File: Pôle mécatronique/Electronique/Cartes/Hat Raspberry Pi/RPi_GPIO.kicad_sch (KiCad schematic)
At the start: 1 part, among them J2 RPi_GPIO

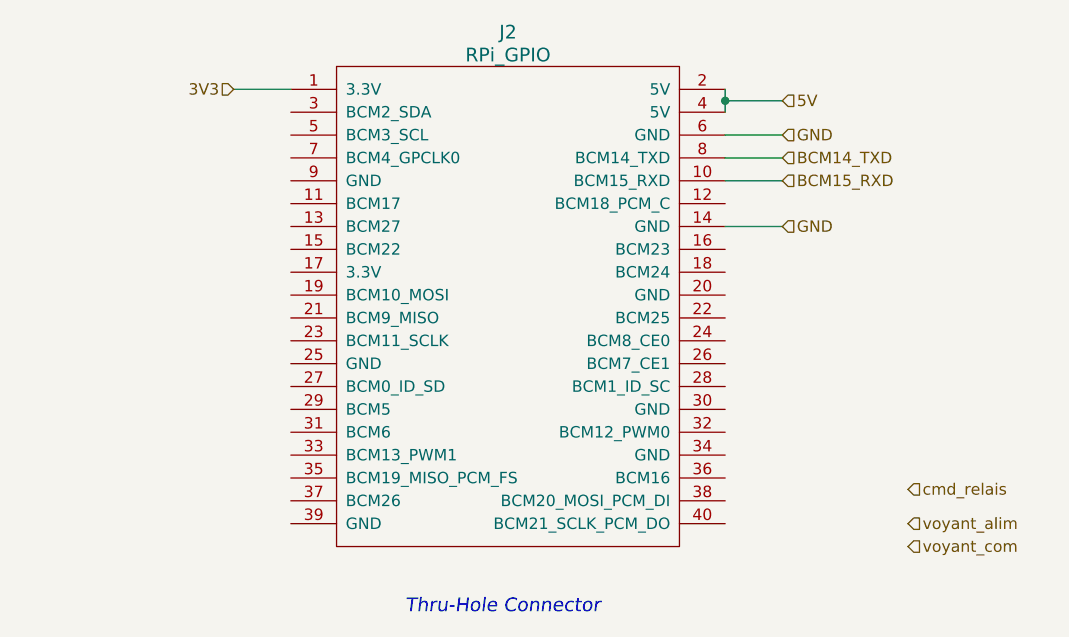
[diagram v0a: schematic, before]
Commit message: Update HAT RPI
- Ajout MCP25625
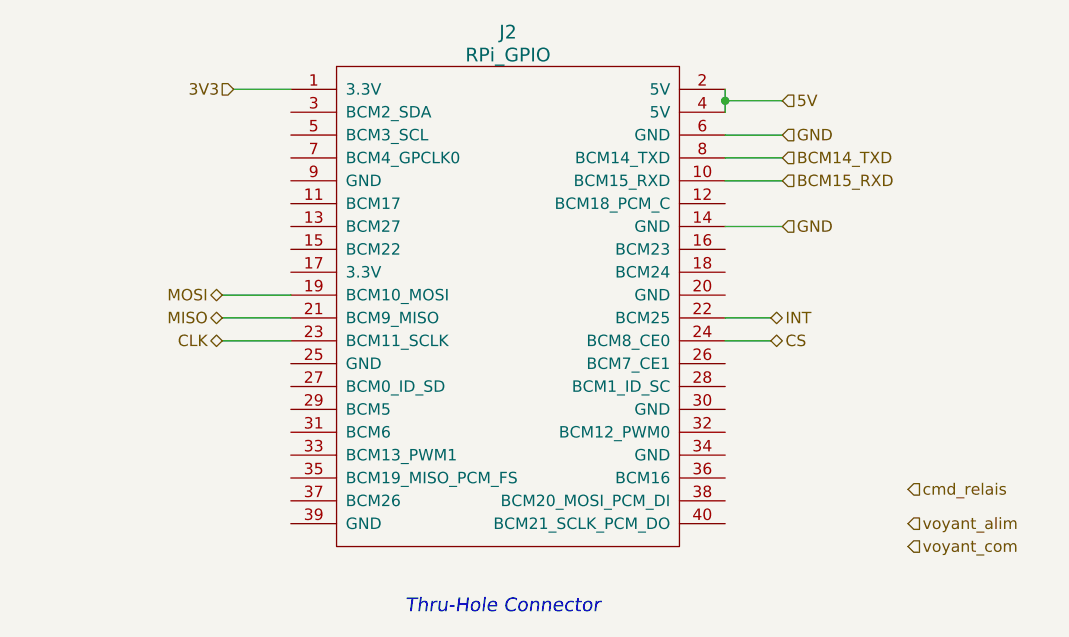
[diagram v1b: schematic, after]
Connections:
- net MOSI: now reaches J2.19 (BCM10_MOSI)
- net MISO: now reaches J2.21 (BCM9_MISO)
- net INT: now reaches J2.22 (BCM25)
- net CLK: now reaches J2.23 (BCM11_SCLK)
- net CS: now reaches J2.24 (BCM8_CE0)
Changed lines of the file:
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@@
+    (stroke (width 0) (type default) (color 0 0 0 0))
+  )
+  (wire (pts (xy 233.68 93.98) (xy 238.76 93.98))
     (stroke (width 0) (type default) (color 0 0 0 0))
   )
@@
     (stroke (width 0) (type default) (color 0 0 0 0))
   )
+  (wire (pts (xy 177.8 91.44) (xy 185.42 91.44))
+    (stroke (width 0) (type default) (color 0 0 0 0))
+  )
   (wire (pts (xy 233.68 68.58) (xy 233.68 69.85))
     (stroke (width 0) (type default) (color 0 0 0 0))
   )
+  (wire (pts (xy 177.8 96.52) (xy 185.42 96.52))
+    (stroke (width 0) (type default) (color 0 0 0 0))
+  )
   (wire (pts (xy 233.68 73.66) (xy 240.03 73.66))
+    (stroke (width 0) (type default) (color 0 0 0 0))
+  )
+  (wire (pts (xy 177.8 93.98) (xy 185.42 93.98))
     (stroke (width 0) (type default) (color 0 0 0 0))
   )
@@
   )
   (wire (pts (xy 233.68 69.85) (xy 233.68 71.12))
+    (stroke (width 0) (type default) (color 0 0 0 0))
+  )
+  (wire (pts (xy 233.68 96.52) (xy 238.76 96.52))
     (stroke (width 0) (type default) (color 0 0 0 0))
   )
@@
     (effects (font (size 1.27 1.27)) (justify left))
   )
+  (hierarchical_label "INT" (shape bidirectional) (at 238.76 93.98 0)
+    (effects (font (size 1.27 1.27)) (justify left))
+  )
   (hierarchical_label "BCM14_TXD" (shape input) (at 240.03 76.2 0)
     (effects (font (size 1.27 1.27)) (justify left))
+  )
+  (hierarchical_label "CS" (shape bidirectional) (at 238.76 96.52 0)
+    (effects (font (size 1.27 1.27)) (justify left))
+  )
+  (hierarchical_label "MOSI" (shape bidirectional) (at 177.8 91.44 180)
+    (effects (font (size 1.27 1.27)) (justify right))
   )
   (hierarchical_label "GND" (shape input) (at 240.03 73.66 0)
@@
   (hierarchical_label "cmd_relais" (shape input) (at 254 113.03 0)
     (effects (font (size 1.27 1.27)) (justify left))
+  )
+  (hierarchical_label "CLK" (shape bidirectional) (at 177.8 96.52 180)
+    (effects (font (size 1.27 1.27)) (justify right))
   )
   (hierarchical_label "voyant_alim" (shape input) (at 254 116.84 0)
@@
     (effects (font (size 1.27 1.27)) (justify left))
   )
+  (hierarchical_label "MISO" (shape bidirectional) (at 177.8 93.98 180)
+    (effects (font (size 1.27 1.27)) (justify right))
+  )
   (hierarchical_label "5V" (shape input) (at 240.03 69.85 0)

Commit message: Update HAT
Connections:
- net GND: now also J2.25 (GND), J2.39 (GND), J2.9 (GND); no longer J2.14 (GND)
- net cmd_relais: now also J2.7 (BCM4_GPCLK0)
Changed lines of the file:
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@@
     (stroke (width 0) (type default) (color 0 0 0 0))
   )
-  (wire (pts (xy 233.68 83.82) (xy 240.03 83.82))
+  (wire (pts (xy 180.34 78.74) (xy 185.42 78.74))
     (stroke (width 0) (type default) (color 0 0 0 0))
   )
@@
     (stroke (width 0) (type default) (color 0 0 0 0))
   )
+  (wire (pts (xy 180.34 76.2) (xy 185.42 76.2))
+    (stroke (width 0) (type default) (color 0 0 0 0))
+  )
+  (wire (pts (xy 180.34 99.06) (xy 185.42 99.06))
+    (stroke (width 0) (type default) (color 0 0 0 0))
+  )
   (wire (pts (xy 177.8 93.98) (xy 185.42 93.98))
+    (stroke (width 0) (type default) (color 0 0 0 0))
+  )
+  (wire (pts (xy 181.61 116.84) (xy 185.42 116.84))
     (stroke (width 0) (type default) (color 0 0 0 0))
   )
@@
     (effects (font (size 1.27 1.27)) (justify left))
   )
-  (hierarchical_label "GND" (shape input) (at 240.03 83.82 0)
+  (hierarchical_label "INT" (shape bidirectional) (at 238.76 93.98 0)
     (effects (font (size 1.27 1.27)) (justify left))
   )
-  (hierarchical_label "INT" (shape bidirectional) (at 238.76 93.98 0)
-    (effects (font (size 1.27 1.27)) (justify left))
+  (hierarchical_label "GND" (shape input) (at 180.34 78.74 180)
+    (effects (font (size 1.27 1.27)) (justify right))
   )
   (hierarchical_label "BCM14_TXD" (shape input) (at 240.03 76.2 0)
@@
     (effects (font (size 1.27 1.27)) (justify left))
   )
-  (hierarchical_label "cmd_relais" (shape input) (at 254 113.03 0)
-    (effects (font (size 1.27 1.27)) (justify left))
+  (hierarchical_label "cmd_relais" (shape input) (at 180.34 76.2 180)
+    (effects (font (size 1.27 1.27)) (justify right))
+  )
+  (hierarchical_label "GND" (shape input) (at 180.34 99.06 180)
+    (effects (font (size 1.27 1.27)) (justify right))
   )
   (hierarchical_label "CLK" (shape bidirectional) (at 177.8 96.52 180)
     (effects (font (size 1.27 1.27)) (justify right))
   )
-  (hierarchical_label "voyant_alim" (shape input) (at 254 116.84 0)
-    (effects (font (size 1.27 1.27)) (justify left))
-  )
   (hierarchical_label "3V3" (shape input) (at 179.07 68.58 180)
     (effects (font (size 1.27 1.27)) (justify right))
   )
-  (hierarchical_label "voyant_com" (shape input) (at 254 119.38 0)
-    (effects (font (size 1.27 1.27)) (justify left))
+  (hierarchical_label "GND" (shape input) (at 181.61 116.84 180)
+    (effects (font (size 1.27 1.27)) (justify right))
   )
   (hierarchical_label "MISO" (shape bidirectional) (at 177.8 93.98 180)

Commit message: Update alim correction
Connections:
- net GND: no longer J2.39 (GND)
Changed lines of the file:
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@@
-    (stroke (width 0) (type default) (color 0 0 0 0))
-  )
-  (wire (pts (xy 181.61 116.84) (xy 185.42 116.84))
     (stroke (width 0) (type default) (color 0 0 0 0))
   )
@@
     (effects (font (size 1.27 1.27)) (justify right))
   )
-  (hierarchical_label "GND" (shape input) (at 181.61 116.84 180)
-    (effects (font (size 1.27 1.27)) (justify right))
-  )

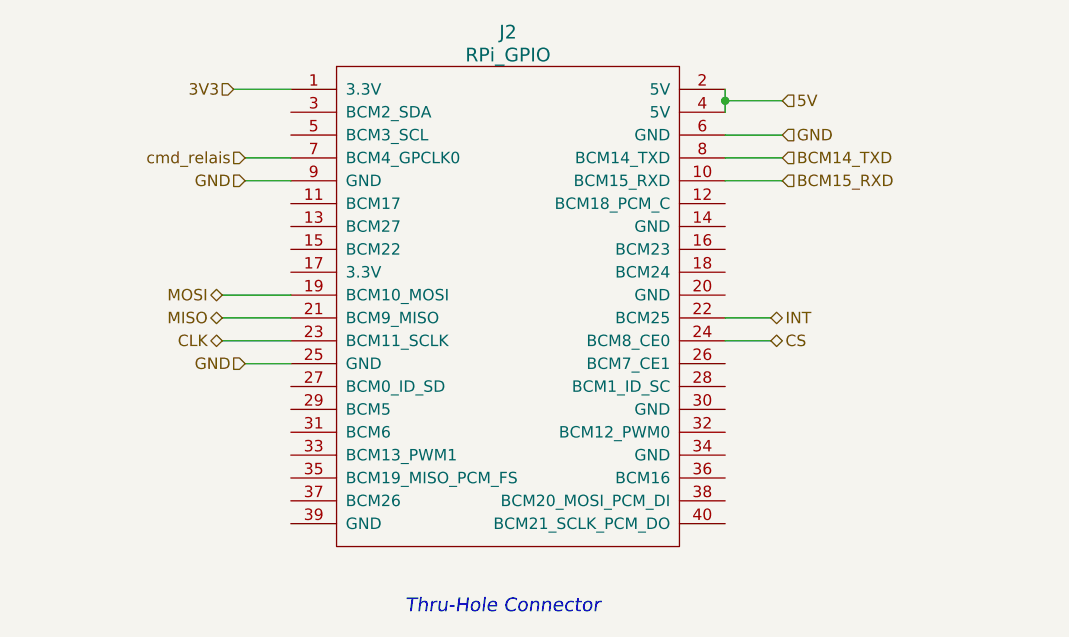
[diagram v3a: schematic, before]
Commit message: Update HAT
- Ajout des pads
- Correction du schéma
- Corrections diverses
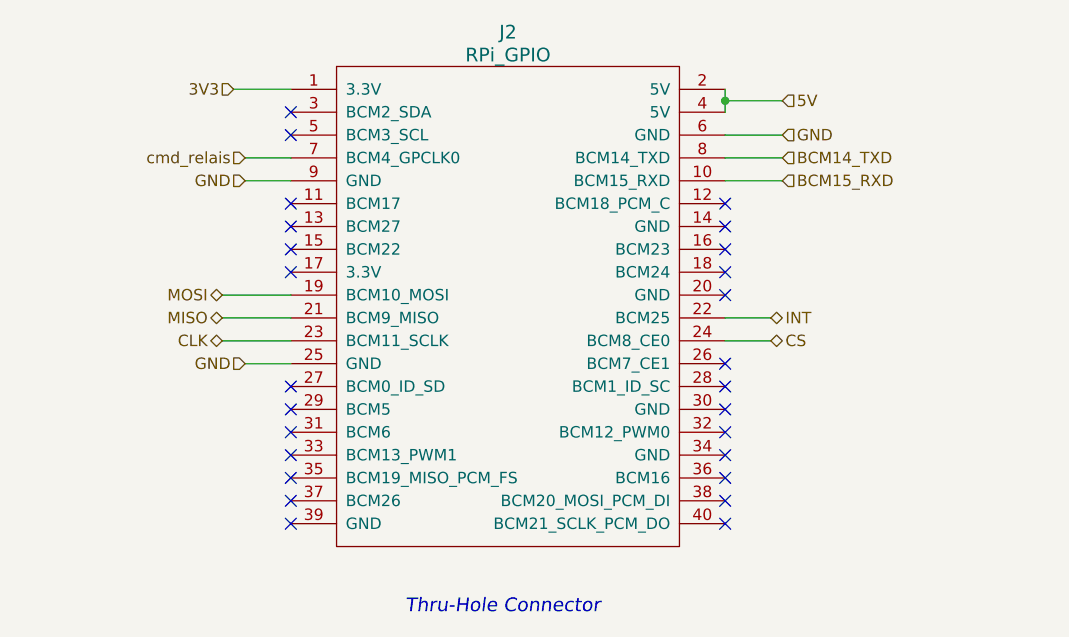
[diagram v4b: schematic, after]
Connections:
- no-connect marks 0 -> 26
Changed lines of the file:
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@@
   (junction (at 233.68 69.85) (diameter 0) (color 0 0 0 0)
   )
+  (no_connect (at 185.42 116.84))
+  (no_connect (at 185.42 114.3))
+  (no_connect (at 185.42 111.76))
+  (no_connect (at 185.42 106.68))
+  (no_connect (at 185.42 104.14))
+  (no_connect (at 185.42 101.6))
+  (no_connect (at 185.42 73.66))
+  (no_connect (at 185.42 71.12))
+  (no_connect (at 185.42 88.9))
+  (no_connect (at 185.42 86.36))
+  (no_connect (at 185.42 83.82))
+  (no_connect (at 185.42 81.28))
+  (no_connect (at 185.42 109.22))
+  (no_connect (at 233.68 111.76))
+  (no_connect (at 233.68 114.3))
+  (no_connect (at 233.68 116.84))
+  (no_connect (at 233.68 86.36))
+  (no_connect (at 233.68 88.9))
+  (no_connect (at 233.68 91.44))
+  (no_connect (at 233.68 81.28))
+  (no_connect (at 233.68 83.82))
+  (no_connect (at 233.68 99.06))
+  (no_connect (at 233.68 101.6))
+  (no_connect (at 233.68 104.14))
+  (no_connect (at 233.68 106.68))
+  (no_connect (at 233.68 109.22))
   (wire (pts (xy 179.07 68.58) (xy 185.42 68.58))
     (stroke (width 0) (type default) (color 0 0 0 0))

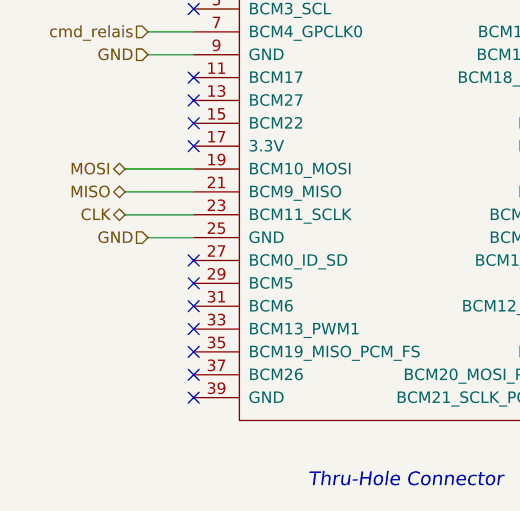
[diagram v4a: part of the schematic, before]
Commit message: Update HAT & Archi
HAT : - Ajout de l'interrupteur logique de démarrage

Archi : - Update générale
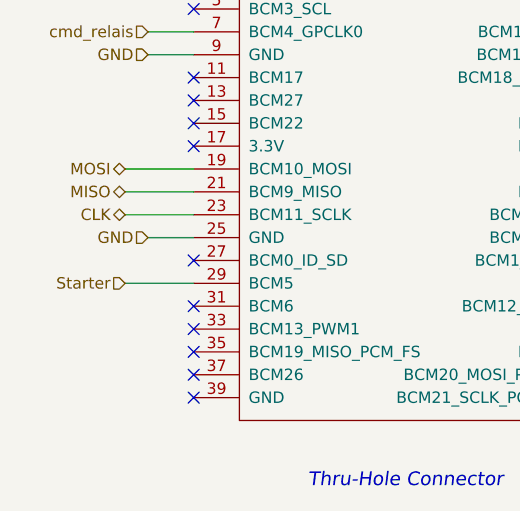
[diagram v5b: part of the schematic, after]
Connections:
- net Starter: now reaches J2.29 (BCM5)
- no-connect marks 26 -> 25
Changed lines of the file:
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@@
   (no_connect (at 185.42 111.76))
   (no_connect (at 185.42 106.68))
-  (no_connect (at 185.42 104.14))
   (no_connect (at 185.42 101.6))
   (no_connect (at 185.42 73.66))
@@
   )
   (wire (pts (xy 177.8 96.52) (xy 185.42 96.52))
+    (stroke (width 0) (type default) (color 0 0 0 0))
+  )
+  (wire (pts (xy 177.8 104.14) (xy 185.42 104.14))
     (stroke (width 0) (type default) (color 0 0 0 0))
   )
@@
     (effects (font (size 1.27 1.27)) (justify right))
   )
+  (hierarchical_label "Starter" (shape input) (at 177.8 104.14 180)
+    (effects (font (size 1.27 1.27)) (justify right))
+  )

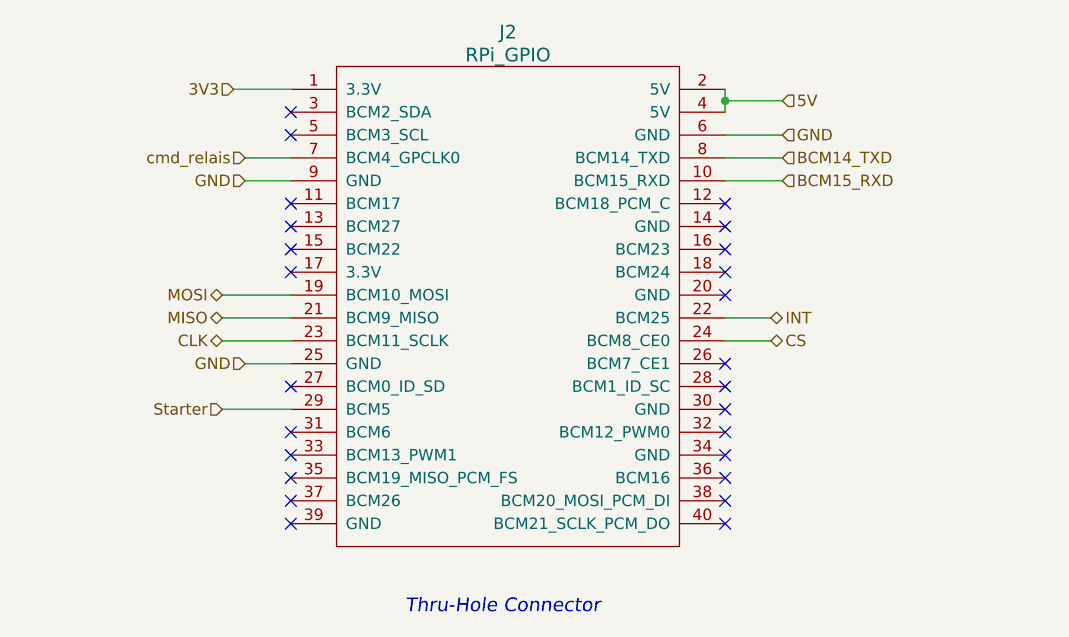
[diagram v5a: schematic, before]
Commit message: Udpate HAT
Sérigraphie
Points de tests
Arret d'urgence
I2C
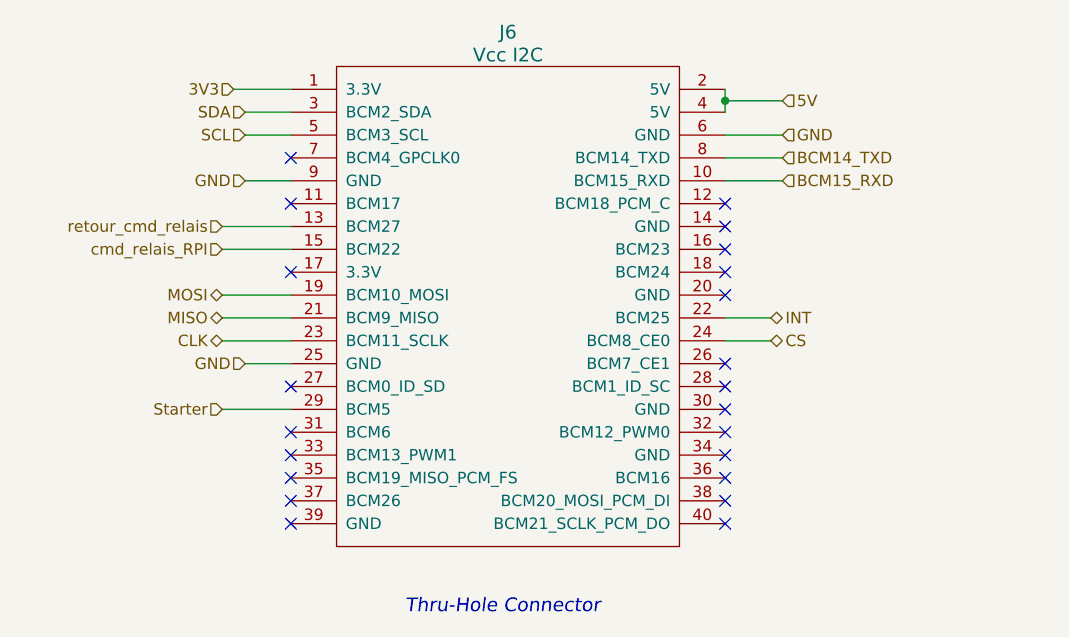
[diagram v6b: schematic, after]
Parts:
- J6: renamed from J2; value RPi_GPIO -> Vcc I2C; footprint RPi_Hat:Pin_Header_Straight_2x20 -> Connector_PinHeader_2.54mm:PinHeader_2x02_P2.54mm_Vertical
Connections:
- net retour_cmd_relais: now reaches J6.13 (BCM27)
- net cmd_relais_RPI: now reaches J6.15 (BCM22)
- net SDA: now reaches J6.3 (BCM2_SDA)
- net SCL: now reaches J6.5 (BCM3_SCL)
- net cmd_relais: no longer names the net of J6.7 (BCM4_GPCLK0)
- no-connect marks 25 -> 22
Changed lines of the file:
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@@
   (no_connect (at 185.42 106.68))
   (no_connect (at 185.42 101.6))
-  (no_connect (at 185.42 73.66))
-  (no_connect (at 185.42 71.12))
   (no_connect (at 185.42 88.9))
-  (no_connect (at 185.42 86.36))
-  (no_connect (at 185.42 83.82))
   (no_connect (at 185.42 81.28))
   (no_connect (at 185.42 109.22))
@@
   (no_connect (at 233.68 106.68))
   (no_connect (at 233.68 109.22))
+  (no_connect (at 185.42 76.2))
   (wire (pts (xy 179.07 68.58) (xy 185.42 68.58))
     (stroke (width 0) (type default) (color 0 0 0 0))
@@
   )
   (wire (pts (xy 180.34 78.74) (xy 185.42 78.74))
+    (stroke (width 0) (type default) (color 0 0 0 0))
+  )
+  (wire (pts (xy 177.8 86.36) (xy 185.42 86.36))
+    (stroke (width 0) (type default) (color 0 0 0 0))
+  )
+  (wire (pts (xy 180.34 71.12) (xy 185.42 71.12))
     (stroke (width 0) (type default) (color 0 0 0 0))
   )
@@
     (stroke (width 0) (type default) (color 0 0 0 0))
   )
+  (wire (pts (xy 180.34 73.66) (xy 185.42 73.66))
+    (stroke (width 0) (type default) (color 0 0 0 0))
+  )
   (wire (pts (xy 233.68 73.66) (xy 240.03 73.66))
     (stroke (width 0) (type default) (color 0 0 0 0))
   )
-  (wire (pts (xy 180.34 76.2) (xy 185.42 76.2))
+  (wire (pts (xy 177.8 83.82) (xy 185.42 83.82))
     (stroke (width 0) (type default) (color 0 0 0 0))
   )
@@
     (effects (font (size 1.27 1.27)) (justify left))
   )
+  (hierarchical_label "SDA" (shape input) (at 180.34 71.12 180)
+    (effects (font (size 1.27 1.27)) (justify right))
+  )
+  (hierarchical_label "SCL" (shape input) (at 180.34 73.66 180)
+    (effects (font (size 1.27 1.27)) (justify right))
+  )
+  (hierarchical_label "cmd_relais_RPI" (shape input) (at 177.8 86.36 180)
+    (effects (font (size 1.27 1.27)) (justify right))
+  )
   (hierarchical_label "INT" (shape bidirectional) (at 238.76 93.98 0)
     (effects (font (size 1.27 1.27)) (justify left))
@@
     (effects (font (size 1.27 1.27)) (justify left))
   )
-  (hierarchical_label "cmd_relais" (shape input) (at 180.34 76.2 180)
-    (effects (font (size 1.27 1.27)) (justify right))
-  )
   (hierarchical_label "GND" (shape input) (at 180.34 99.06 180)
     (effects (font (size 1.27 1.27)) (justify right))
@@
   )
   (hierarchical_label "Starter" (shape input) (at 177.8 104.14 180)
+    (effects (font (size 1.27 1.27)) (justify right))
+  )
+  (hierarchical_label "retour_cmd_relais" (shape input) (at 177.8 83.82 180)
     (effects (font (size 1.27 1.27)) (justify right))
   )
@@
   (symbol (lib_id "RPi_Hat:RPi_GPIO") (at 190.5 68.58 0) (unit 1)
     (in_bom yes) (on_board yes)
-    (property "Reference" "J2" (id 0) (at 209.55 62.23 0)
+    (property "Reference" "J6" (id 0) (at 209.55 62.23 0)
       (effects (font (size 1.524 1.524)))
     )
-    (property "Value" "RPi_GPIO" (id 1) (at 209.55 64.77 0)
+    (property "Value" "Vcc I2C" (id 1) (at 209.55 64.77 0)
       (effects (font (size 1.524 1.524)))
     )
-    (property "Footprint" "RPi_Hat:Pin_Header_Straight_2x20" (id 2) (at 190.5 68.58 0)
+    (property "Footprint" "Connector_PinHeader_2.54mm:PinHeader_2x02_P2.54mm_Vertical" (id 2) (at 190.5 68.58 0)
       (effects (font (size 1.524 1.524)) hide)
     )
